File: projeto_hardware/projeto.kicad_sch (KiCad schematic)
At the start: 111 parts, among them J1 arrego, J2 Conn_01x08_Pin, P1 Card_SD, Q1 BC847, Q2 BC847, SW1 SW_DPST_x2, SW2 SW_DPST_x2, SW3 SW_DPST_x2, SW5 SW_DPST_x2, SW6 SW_DPDT_x2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

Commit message: falta só fazer as trilhas praticamente
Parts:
- removed D1: SS14, Diode_SMD:D_SMA, symbol Diode:SS14
- removed J2: Conn_01x08_Pin, Connector_PinHeader_2.54mm:PinHeader_1x08_P2.54mm_Vertical, symbol Connector:Conn_01x08_Pin
- removed TP22: TP_BZR, TestPoint:TestPoint_Pad_D1.0mm, symbol Connector:TestPoint
- removed TP31: TP_ENC1_E, TestPoint:TestPoint_Pad_D1.0mm, symbol Connector:TestPoint
- removed TP32: TP_ENC2_E, TestPoint:TestPoint_Pad_D1.0mm, symbol Connector:TestPoint
- removed TP33: TP_ENC1_D, TestPoint:TestPoint_Pad_D1.0mm, symbol Connector:TestPoint
- removed TP34: TP_ENC2_D, TestPoint:TestPoint_Pad_D1.0mm, symbol Connector:TestPoint
- added D1: LED, Resistor_SMD:R_0805_2012Metric_Pad1.20x1.40mm_HandSolder, symbol Device:LED
- added J3: Conn_01x10_Pin, Connector_PinHeader_2.54mm:PinHeader_1x10_P2.54mm_Vertical, symbol Connector:Conn_01x10_Pin
- added R31: 220, Resistor_SMD:R_0805_2012Metric_Pad1.20x1.40mm_HandSolder, symbol Device:R
- BZ1: footprint Buzzer_Beeper:Buzzer_12x9.5RM7.6 -> Library:MagneticBuzzer_CUI_CMT-8504-100-SMT_3d
- SW1: value SW_DPST_x2 -> BOOT
- SW2: value SW_DPST_x2 -> BTN2
- SW3: value SW_DPST_x2 -> RST
- SW5: value SW_DPST_x2 -> BTN1
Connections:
- net +12V: now also SW6.3 (A); no longer SW6.1 (A)
- net +3.3V: now also D1.2 (A), J3.1 (Pin_1)
- net +5V: now also SW6.1 (C); no longer SW6.3 (C)
- net BTN_1: now also U1.4 (GPIO4/TOUCH4/ADC1_CH3)
- net BTN_2: now also U1.5 (GPIO5/TOUCH5/ADC1_CH4)
- net BZR: now also U1.29 (SPIIO7/GPIO36/FSPICLK/SUBSPICLK)
- net CS: now also U1.9 (GPIO16/U0CTS/ADC2_CH5/XTAL_32K_N)
- net D+: now also U1.14 (GPIO20/U1CTS/ADC2_CH9/CLK_OUT1/USB_D+); no longer U1.21 (GPIO13/TOUCH13/ADC2_CH2/FSPIQ/FSPIIO7/SUBSPIQ)
- net D-: now also U1.13 (GPIO19/U1RTS/ADC2_CH8/CLK_OUT2/USB_D-); no longer U1.20 (GPIO12/TOUCH12/ADC2_CH1/FSPICLK/FSPIIO6/SUBSPICLK)
- net DIV_TENSAO: now also U1.38 (GPIO2/TOUCH2/ADC1_CH1)
- net ENC1_D: now also U1.32 (MTCK/GPIO39/CLK_OUT3/SUBSPICS1)
- net ENC1_E: now also U1.34 (MTDI/GPIO41/CLK_OUT1)
- net ENC2_D: now also U1.33 (MTDO/GPIO40/CLK_OUT2)
- net ENC2_E: now also U1.35 (MTMS/GPIO42)
- net GND: now also J3.10 (Pin_10), R31.2
- net IN1_D: now also U1.17 (GPIO9/TOUCH9/ADC1_CH8/FSPIHD/SUBSPIHD)
- net IN1_E: now also U1.23 (GPIO21)
- net IN2_D: now also U1.15 (GPIO3/TOUCH3/ADC1_CH2)
- net IN2_E: now also U1.24 (GPIO47/SPICLK_P/SUBSPICLK_P_DIFF)
- net MISO: now also U1.6 (GPIO6/TOUCH6/ADC1_CH5)
- net MOSI: now also U1.8 (GPIO15/U0RTS/ADC2_CH4/XTAL_32K_P)
- net S0: now also U1.20 (GPIO12/TOUCH12/ADC2_CH1/FSPICLK/FSPIIO6/SUBSPICLK)
- net S1: now also U1.19 (GPIO11/TOUCH11/ADC2_CH0/FSPID/FSPIIO5/SUBSPID)
- net S2: now also U1.18 (GPIO10/TOUCH10/ADC1_CH9/FSPICS0/FSPIIO4/SUBSPICS0)
- net SCK: now also U1.7 (GPIO7/TOUCH7/ADC1_CH6)
- net SCL: now also U1.10 (GPIO17/U1TXD/ADC2_CH6)
- net SDA: now also U1.11 (GPIO18/U1RXD/ADC2_CH7/CLK_OUT3)
- net SD_digital: now also U1.25 (GPIO48/SPICLK_N/SUBSPICLK_N_DIFF)
- net SE_digital: now also U1.28 (SPIIO6/GPIO35/FSPID/SUBSPID)
- net SIG: now also U1.21 (GPIO13/TOUCH13/ADC2_CH2/FSPIQ/FSPIIO7/SUBSPIQ)
- net Vin: now also SW6.2 (B), SW6.5 (B)
- net i_D: now also U1.12 (GPIO8/TOUCH8/ADC1_CH7/SUBSPICS1)
- net i_E: now also U1.22 (GPIO14/TOUCH14/ADC2_CH3/FSPIWP/FSPIDQS/SUBSPIWP)
- net at U11.1 (X4): now also J3.5 (Pin_5)
- net at U11.12 (X3): now also J3.6 (Pin_6)
- net at U11.13 (X0): now also J3.9 (Pin_9)
- net at U11.14 (X1): now also J3.8 (Pin_8)
- net at U11.15 (X2): now also J3.7 (Pin_7)
- net at U11.2 (X6): now also J3.3 (Pin_3)
- net at U11.4 (X7): now also J3.2 (Pin_2)
- net at U11.5 (X5): now also J3.4 (Pin_4)
- new net: D1.1 (K), R31.1
- no-connect marks 7 -> 10

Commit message: pronto - só revisar com calma
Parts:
- removed TP1: TP_12v, TestPoint:TestPoint_Pad_D1.0mm, symbol Connector:TestPoint
- removed TP12: TP_IN1_E, TestPoint:TestPoint_Pad_D1.0mm, symbol Connector:TestPoint
- removed TP13: TP_IN2_E, TestPoint:TestPoint_Pad_D1.0mm, symbol Connector:TestPoint
- removed TP14: TP_IN2_D, TestPoint:TestPoint_Pad_D1.0mm, symbol Connector:TestPoint
- removed TP15: TP_IN1_D, TestPoint:TestPoint_Pad_D1.0mm, symbol Connector:TestPoint
- removed TP2: TP_GND, TestPoint:TestPoint_Pad_D1.0mm, symbol Connector:TestPoint
- removed TP23: TP_SE, TestPoint:TestPoint_Pad_D1.0mm, symbol Connector:TestPoint
- removed TP24: TP_SD, TestPoint:TestPoint_Pad_D1.0mm, symbol Connector:TestPoint
- removed TP3: TP_3.3V, TestPoint:TestPoint_Pad_D1.0mm, symbol Connector:TestPoint
- removed TP4: TP_5V, TestPoint:TestPoint_Pad_D1.0mm, symbol Connector:TestPoint
- removed TP5: TP_ME1, TestPoint:TestPoint_Pad_D1.0mm, symbol Connector:TestPoint
- removed TP6: TP_ME2, TestPoint:TestPoint_Pad_D1.0mm, symbol Connector:TestPoint
- removed TP7: TP_MD1, TestPoint:TestPoint_Pad_D1.0mm, symbol Connector:TestPoint
- removed TP8: TP_MD2, TestPoint:TestPoint_Pad_D1.0mm, symbol Connector:TestPoint
- removed TP9: TP_VM, TestPoint:TestPoint_Pad_D1.0mm, symbol Connector:TestPoint
- added J2, J4, J5: arrego, Connector_PinHeader_2.54mm:PinHeader_1x01_P2.54mm_Vertical, symbol Connector:Conn_01x01_Pin
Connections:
- net IN1_D: now also U1.15 (GPIO3/TOUCH3/ADC1_CH2); no longer U1.17 (GPIO9/TOUCH9/ADC1_CH8/FSPIHD/SUBSPIHD)
- net IN2_D: now also U1.17 (GPIO9/TOUCH9/ADC1_CH8/FSPIHD/SUBSPIHD); no longer U1.15 (GPIO3/TOUCH3/ADC1_CH2)
- net at U1.30 (SPIDQS/GPIO37/FSPIQ/SUBSPIQ): now also J5.1 (Pin_1)
- net at U1.31 (GPIO38/FSPIWP/SUBSPIWP): now also J4.1 (Pin_1)
- net at U1.39 (GPIO1/TOUCH1/ADC1_CH0): now also J2.1 (Pin_1)
- no-connect marks 10 -> 7

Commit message: parafuso m2 - div tensao 1/8W
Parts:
- R22, R25: footprint Resistor_SMD:R_1206_3216Metric -> Resistor_SMD:R_0805_2012Metric_Pad1.20x1.40mm_HandSolder
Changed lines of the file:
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@@
 			)
 		)
-		(property "Footprint" "Resistor_SMD:R_1206_3216Metric"
+		(property "Footprint" "Resistor_SMD:R_0805_2012Metric_Pad1.20x1.40mm_HandSolder"
 			(at 212.09 195.072 90)
 			(effects
@@
 			)
 		)
-		(property "Footprint" "Resistor_SMD:R_1206_3216Metric"
+		(property "Footprint" "Resistor_SMD:R_0805_2012Metric_Pad1.20x1.40mm_HandSolder"
 			(at 222.25 195.072 90)
 			(effects

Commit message: projeto step
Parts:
- removed P1: Card_SD, Library:Micro_SD_card, symbol ST-TF-003A:ST-TF-003A
- added J6: MEM2075-00-140-01-A, Library:MEM2075-00-140-01-A_GCT, symbol 2026-03-26_23-56-39:MEM2075-00-140-01-A
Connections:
- net +3.3V: now also J6.P4 (VDD)
- net CD: now also J6.P9 (CD)
- net CS: now also J6.P2 (DAT3)
- net GND: now also J6.10 (GND), J6.11 (GND), J6.12 (GND), J6.13 (GND), J6.14 (GND), J6.15 (GND), J6.P6 (VSS)
- net MISO: now also J6.P7 (DAT0)
- net MOSI: now also J6.P3 (CMD)
- net SCK: now also J6.P5 (CLK)

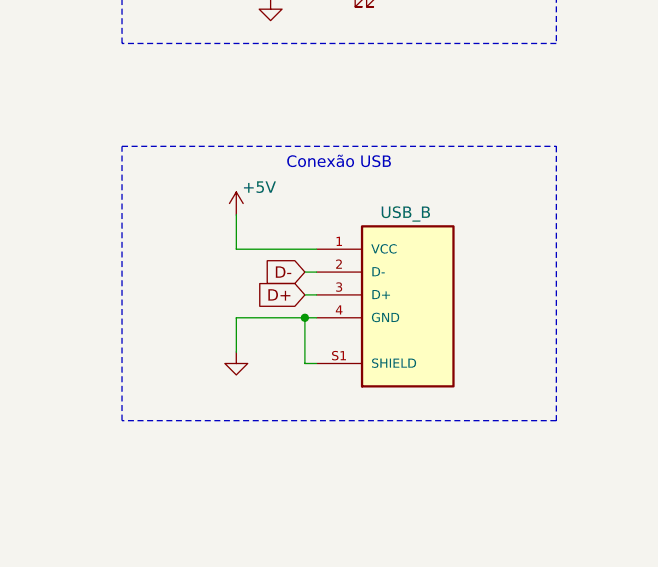
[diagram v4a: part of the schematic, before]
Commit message: add resitor 22 ohms no USB
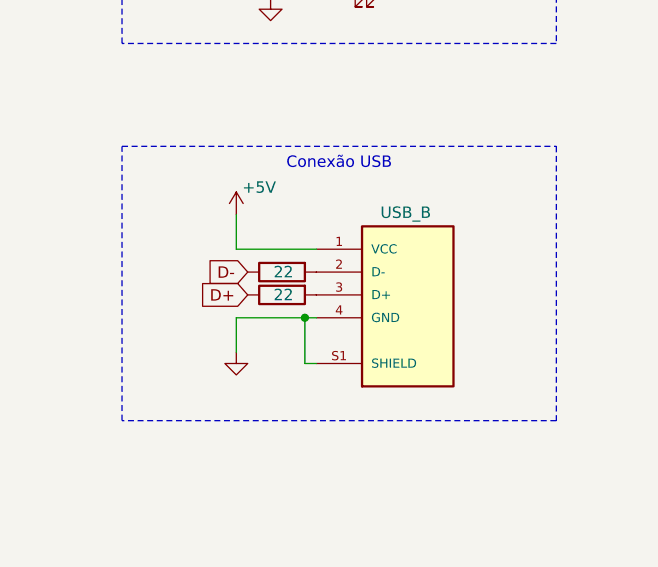
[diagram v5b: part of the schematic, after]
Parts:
- added R32, R33: 22, Resistor_SMD:R_0805_2012Metric_Pad1.20x1.40mm_HandSolder, symbol Device:R
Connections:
- net D+: now also R33.1; no longer USB-B-S-X-X-TH1.3 (D+)
- net D-: now also R32.1; no longer USB-B-S-X-X-TH1.2 (D-)
- new net: R33.2, USB-B-S-X-X-TH1.3 (D+)
- new net: R32.2, USB-B-S-X-X-TH1.2 (D-)
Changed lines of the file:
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@@
 	(wire
 		(pts
-			(xy 46.99 240.03) (xy 48.26 240.03)
-		)
-		(stroke
-			(width 0)
-			(type default)
-		)
-	)
-	(wire
-		(pts
 			(xy 274.32 219.71) (xy 274.32 222.25)
 		)
@@
 	(wire
 		(pts
-			(xy 46.99 242.57) (xy 48.26 242.57)
-		)
-		(stroke
-			(width 0)
-			(type default)
-		)
-	)
-	(wire
-		(pts
 			(xy 279.4 142.24) (xy 279.4 138.43)
 		)
@@
 	(global_label "D-"
 		(shape input)
-		(at 46.99 240.03 180)
+		(at 40.64 240.03 180)
 		(fields_autoplaced yes)
 		(effects
@@
 		)
 		(property "Intersheetrefs" "${INTERSHEET_REFS}"
-			(at 41.1624 240.03 0)
+			(at 34.8124 240.03 0)
 			(effects
 				(font
@@
 	(global_label "D+"
 		(shape input)
-		(at 46.99 242.57 180)
+		(at 40.64 242.57 180)
 		(fields_autoplaced yes)
 		(effects
@@
 		)
 		(property "Intersheetrefs" "${INTERSHEET_REFS}"
-			(at 41.1624 242.57 0)
+			(at 34.8124 242.57 0)
 			(effects
 				(font
@@
 	)
 	(symbol
+		(lib_id "Device:R")
+		(at 44.45 242.57 90)
+		(mirror x)
+		(unit 1)
+		(exclude_from_sim no)
+		(in_bom yes)
+		(on_board yes)
+		(dnp no)
+		(property "Reference" "R33"
+			(at 43.1799 245.11 0)
+			(effects
+				(font
+					(size 1.27 1.27)
+				)
+				(justify left)
+				(hide yes)
+			)
+		)
+		(property "Value" "22"
+			(at 45.72 242.57 90)
+			(effects
+				(font
+					(size 1.27 1.27)
+				)
+				(justify left)
+			)
+		)
+		(property "Footprint" "Resistor_SMD:R_0805_2012Metric_Pad1.20x1.40mm_HandSolder"
+			(at 44.45 240.792 90)
+			(effects
+				(font
+					(size 1.27 1.27)
+				)
+				(hide yes)
+			)
+		)
+		(property "Datasheet" "~"
+			(at 44.45 242.57 0)
+			(effects
+				(font
+					(size 1.27 1.27)
+				)
+				(hide yes)
+			)
+		)
+		(property "Description" "Resistor"
+			(at 44.45 242.57 0)
+			(effects
+				(font
+					(size 1.27 1.27)
+				)
+				(hide yes)
+			)
+		)
+		(pin "1"
+		)
+		(pin "2"
+		)
+		(instances
+			(project "projeto"
+				(path "/56c4d1ac-2b28-4c47-9c0b-b837ed34c3b9"
+					(reference "R33")
+					(unit 1)
+				)
+			)
+		)
+	)
+	(symbol
 		(lib_id "power:GND")
 		(at 387.35 144.78 0)
@@
 					(unit 1)
 				)
+			)
+		)
+	)
+	(symbol
+		(lib_id "Device:R")
+		(at 44.45 240.03 90)
+		(mirror x)
+		(unit 1)
+		(exclude_from_sim no)
+		(in_bom yes)
+		(on_board yes)
+		(dnp no)
+		(property "Reference" "R32"
+			(at 43.1799 242.57 0)
+			(effects
+				(font
+					(size 1.27 1.27)
+				)
+				(justify left)
+				(hide yes)
+			)
+		)
+		(property "Value" "22"
+			(at 45.72 240.03 90)
+			(effects
+				(font
+					(size 1.27 1.27)
+				)
+				(justify left)
+			)
+		)
+		(property "Footprint" "Resistor_SMD:R_0805_2012Metric_Pad1.20x1.40mm_HandSolder"
+			(at 44.45 238.252 90)
+			(effects
+				(font
+					(size 1.27 1.27)
+				)
+				(hide yes)
+			)
+		)
+		(property "Datasheet" "~"
+			(at 44.45 240.03 0)
+			(effects
+				(font
+					(size 1.27 1.27)
+				)
+				(hide yes)
+			)
+		)
+		(property "Description" "Resistor"
+			(at 44.45 240.03 0)
+			(effects
+				(font
+					(size 1.27 1.27)
+				)
+				(hide yes)
+			)
+		)
+		(pin "1"
+		)
+		(pin "2"
+		)
+		(instances
+			(project "projeto"
+				(path "/56c4d1ac-2b28-4c47-9c0b-b837ed34c3b9"
+					(reference "R32")
+					(unit 1)
+				)
